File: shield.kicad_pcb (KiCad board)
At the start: 4 copper layers, 150 x 120 mm, 155 parts, among them J1 NAPPE_ADC1, J10 OLED_SPI_2x8, J13 NAPPE_LOGIC, J14 NAPPE_COM, J2 NAPPE_ADC2, J3 NAPPE_PWM, J4 NAPPE_GPIO1, J5 DEVKIT_C2000_ROW_A, J6 DEVKIT_C2000_ROW_B, J7 ESP32_C6_DEVKITC_1_J1, J8 ESP32_C6_DEVKITC_1_J3, J9 J_PWR_11-25V, U1 LDO_3V3_ISO, U2 NCM3S1205MC, U3 NCM3S1205MC, U4 ER-OLEDM032-1

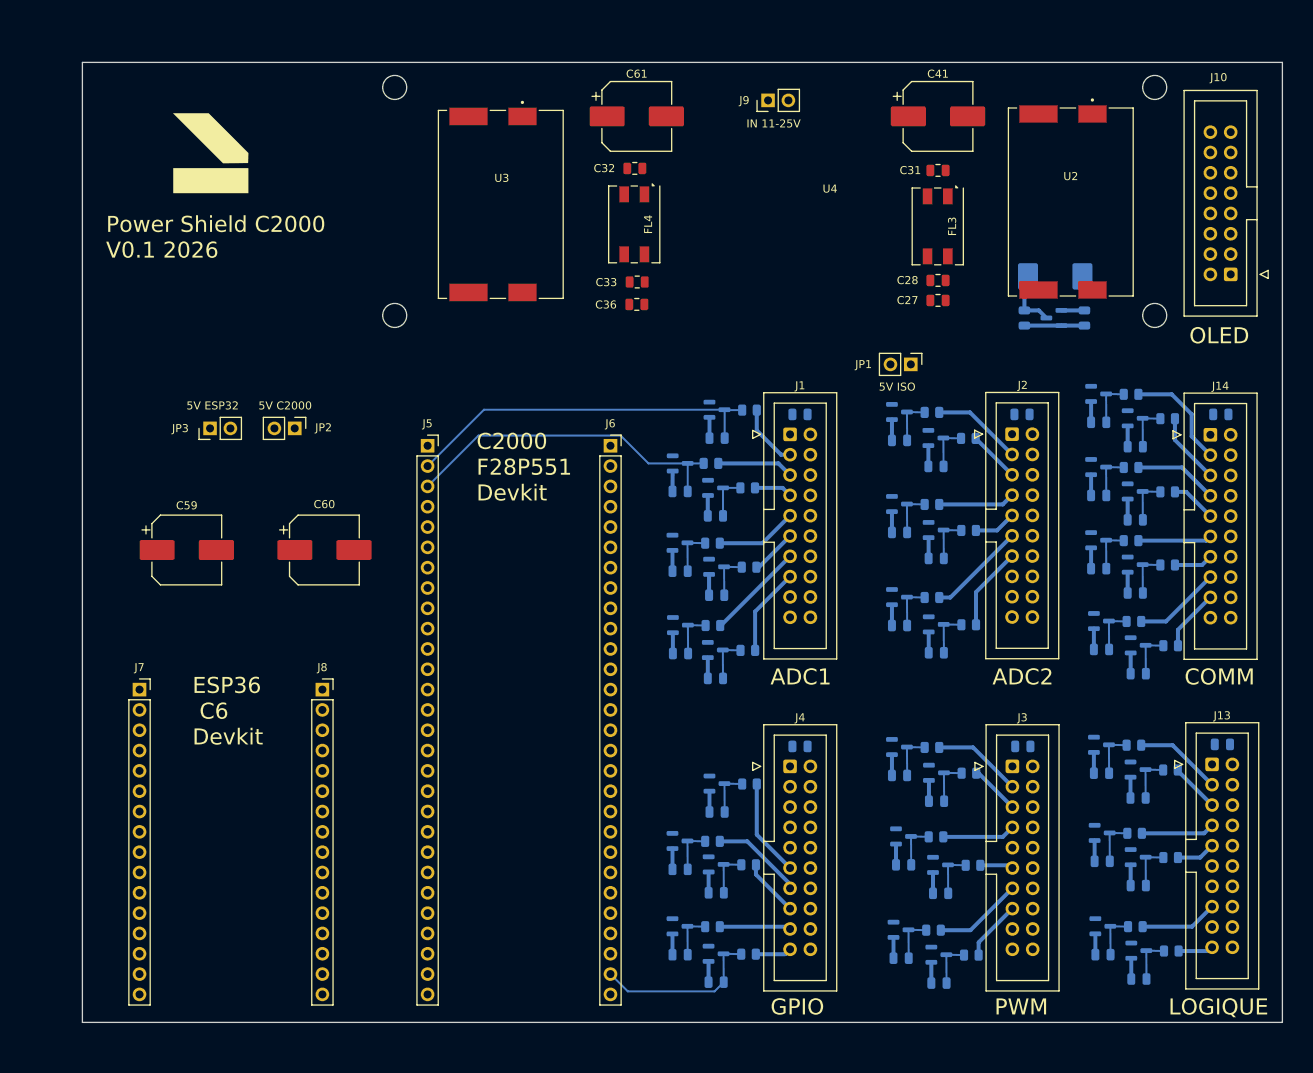
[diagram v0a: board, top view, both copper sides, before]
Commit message: Resauvegarde session KiCad GUI (placement, empreintes USB-C/STUSB4531, PCB)
Checkpoint avant l'ajout des connecteurs dedies carte HV/Filament -
capture l'etat courant de la session KiCad ouverte (reformattage
eeschema, ajustements d'empreinte sur 632722100213 et STUSB4531QTR,
mises a jour PCB/projet) avant toute edition programmatique.
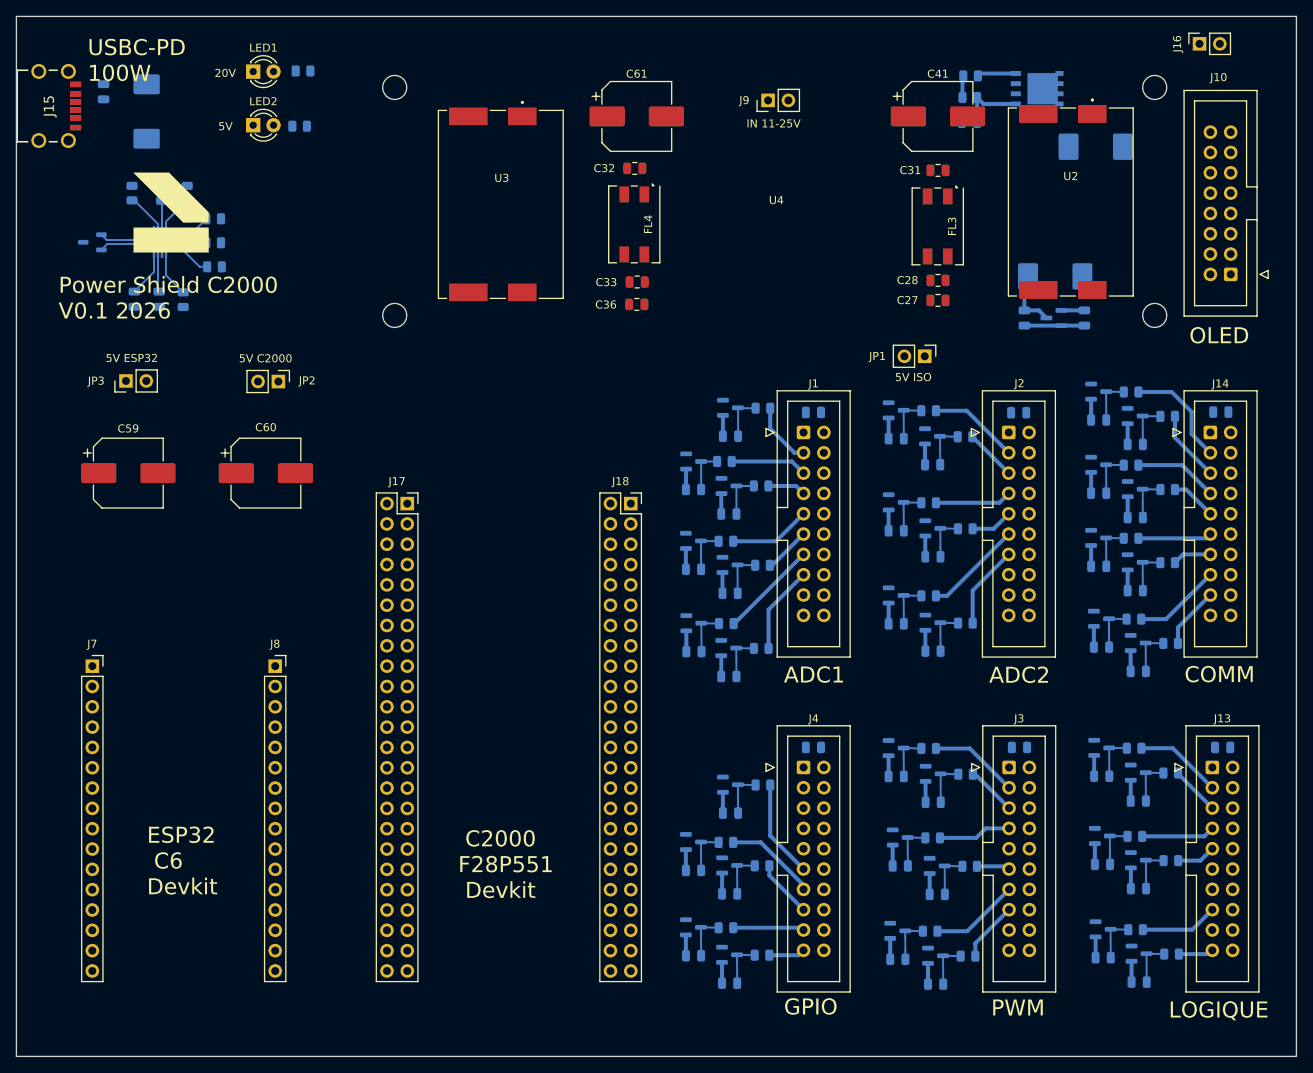
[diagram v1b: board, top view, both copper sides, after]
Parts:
- removed J5: DEVKIT_C2000_ROW_A, Connector_PinSocket_2.54mm:PinSocket_1x28_P2.54mm_Vertical
- removed J6: DEVKIT_C2000_ROW_B, Connector_PinSocket_2.54mm:PinSocket_1x28_P2.54mm_Vertical
- added C62: 4.7uF, Capacitor_SMD:C_0805_2012Metric, B.Cu at (111.9, 37.4)
- added C63: 1uF, Capacitor_SMD:C_0805_2012Metric, B.Cu at (118.8, 63.4)
- added C64: 1uF, Capacitor_SMD:C_0805_2012Metric, B.Cu at (115.8, 63.4)
- added C65: 100nF, Capacitor_SMD:C_0805_2012Metric, B.Cu at (220.1, 41.2)
- added D40: Z3SMCxxx, Diode_SMD:D_SMC, B.Cu at (117.3, 39.9)
- added D41: Z3SMCxxx, Diode_SMD:D_SMC, B.Cu at (235.9, 44.3)
- added D43: ESDA25W, Package_TO_SOT_SMD:SOT-23-3, B.Cu at (110.5, 56.2)
- added J15: USBC-PD, lib:632722100213, F.Cu at (104.8, 39.2)
- added J16: CONN_2PIN, Connector_PinSocket_2.54mm:PinSocket_1x02_P2.54mm_Vertical, F.Cu at (248.9, 31.4)
- added J17: DEVKIT_C2000_A, Connector_PinSocket_2.54mm:PinSocket_2x24_P2.54mm_Vertical, F.Cu at (149.9, 88.9)
- added J18: DEVKIT_C2000_B, Connector_PinSocket_2.54mm:PinSocket_2x24_P2.54mm_Vertical, F.Cu at (177.8, 88.9)
- added LED1: LED, LED_THT:LED_D3.0mm, F.Cu at (130.6, 34.9)
- added LED2: LED, LED_THT:LED_D3.0mm, F.Cu at (130.6, 41.6)
- added Q1: SQJ459EP-T2_GE3, Package_SO:PowerPAK_SO-8_Single, B.Cu at (228.6, 37.0)
- added R39: 1k, Resistor_SMD:R_0805_2012Metric, B.Cu at (125.7, 53.3)
- added R40: 100k, Resistor_SMD:R_0805_2012Metric, B.Cu at (220.3, 35.4)
- added R41: 22k, Resistor_SMD:R_0805_2012Metric, B.Cu at (125.7, 56.3)
- added R42: 100R, Resistor_SMD:R_0805_2012Metric, B.Cu at (220.2, 38.1)
- added R43: 22k, Resistor_SMD:R_0805_2012Metric, B.Cu at (136.8, 34.8)
- added R44: 22k, Resistor_SMD:R_0805_2012Metric, B.Cu at (136.4, 41.7)
- added R45: 4.7k, Resistor_SMD:R_0805_2012Metric, B.Cu at (115.5, 50.1)
- added R46: 4.7k, Resistor_SMD:R_0805_2012Metric, B.Cu at (119.2, 50.1)
- added R47: 4.7k, Resistor_SMD:R_0805_2012Metric, B.Cu at (122.3, 50.1)
- added R48: 1k, Resistor_SMD:R_0805_2012Metric, B.Cu at (125.8, 59.3)
- added R49: 1k, Resistor_SMD:R_0805_2012Metric, B.Cu at (121.8, 63.4)
- added U5: STUSB4531QTR, lib:STUSB4531QTR, B.Cu at (119.0, 56.2)
- moved C59 12.1 mm to (115.0, 85.1)
- moved C60 12.1 mm to (132.2, 85.1)
- moved JP3 12.1 mm to (114.7, 73.6)
- moved Lebel Audio 8.93 mm to (120.6, 52.5)
- moved J7 6.59 mm to (110.5, 109.2)
- moved J8 6.59 mm to (133.3, 109.2)
- moved JP2 6.21 mm to (133.7, 73.6)
- moved JP1 2.01 mm to (214.5, 70.5)
- moved C2 1.70 mm to (185.6, 87.1)
- moved D2 1.70 mm to (185.7, 83.6)
- moved D7 1.70 mm to (185.7, 103.8)
- moved R2 1.70 mm to (189.5, 83.6)
- moved C3 1.70 mm to (190.3, 80.5)
- moved C35 1.70 mm to (200.6, 77.5)
- moved C4 1.70 mm to (185.6, 97.1)
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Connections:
- J8 pad 5: unconnected-(J8-GPIO23-Pad5) -> STUSB_SDA
- J8 pad 6: unconnected-(J8-GPIO22-Pad6) -> STUSB_SCL
- J8 pad 7: unconnected-(J8-GPIO21-Pad7) -> STUSB_ALERT
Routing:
- net Vin_MCU: track 45.8 -> 5.76 mm
- net Vout_MCU: track 42.1 -> 5.50 mm
- net CLB_OUT_MCU: track 21.3 -> 5.76 mm
- net GATE: track 0.00 -> 8.27 mm
- net CC1: track 0.00 -> 6.13 mm
- net CC2: track 0.00 -> 6.09 mm
- net VREG_2V7: track 0.00 -> 5.71 mm
- net STUSB_VBUS_VS_DISCH: track 0.00 -> 5.69 mm
- net STUSB_DISCH: track 0.00 -> 5.58 mm
- net STUSB_SCL: track 0.00 -> 5.22 mm
- net STUSB_ADD0: track 0.00 -> 5.19 mm
- net VBUS_IN: track 0.00 -> 4.87 mm
- net STUSB_ALERT: track 0.00 -> 4.80 mm
- net VREG_1V2: track 0.00 -> 4.76 mm
- net VBUS_EN_SNK: track 0.00 -> 4.44 mm
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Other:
- board size 150 x 120 mm -> 160 x 130 mm
- board text added: "20V"
- board text added: "5V"
- board text added: "ESP32 C6 Devkit"
- board text added: "USBC-PD 100W"
- board text removed: "ESP36 C6 Devkit"
